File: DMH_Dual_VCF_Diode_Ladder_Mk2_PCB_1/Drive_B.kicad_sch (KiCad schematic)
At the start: 25 parts, among them J17 Conn_01x10_PinHeader, Q1 BC548, Q2 BC548, U1 TL074

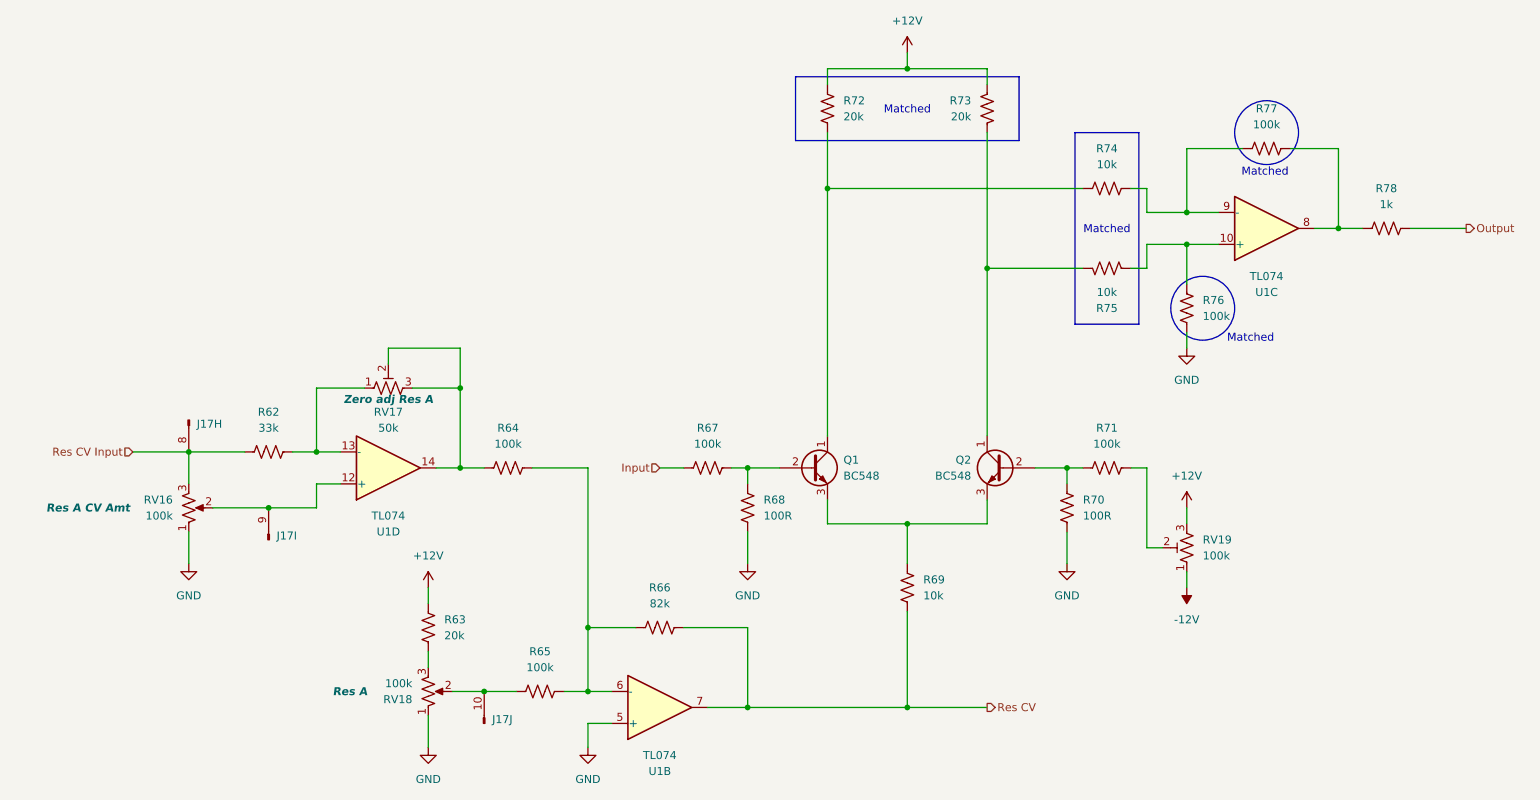
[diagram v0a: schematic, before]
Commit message: Created Drive CV circuits
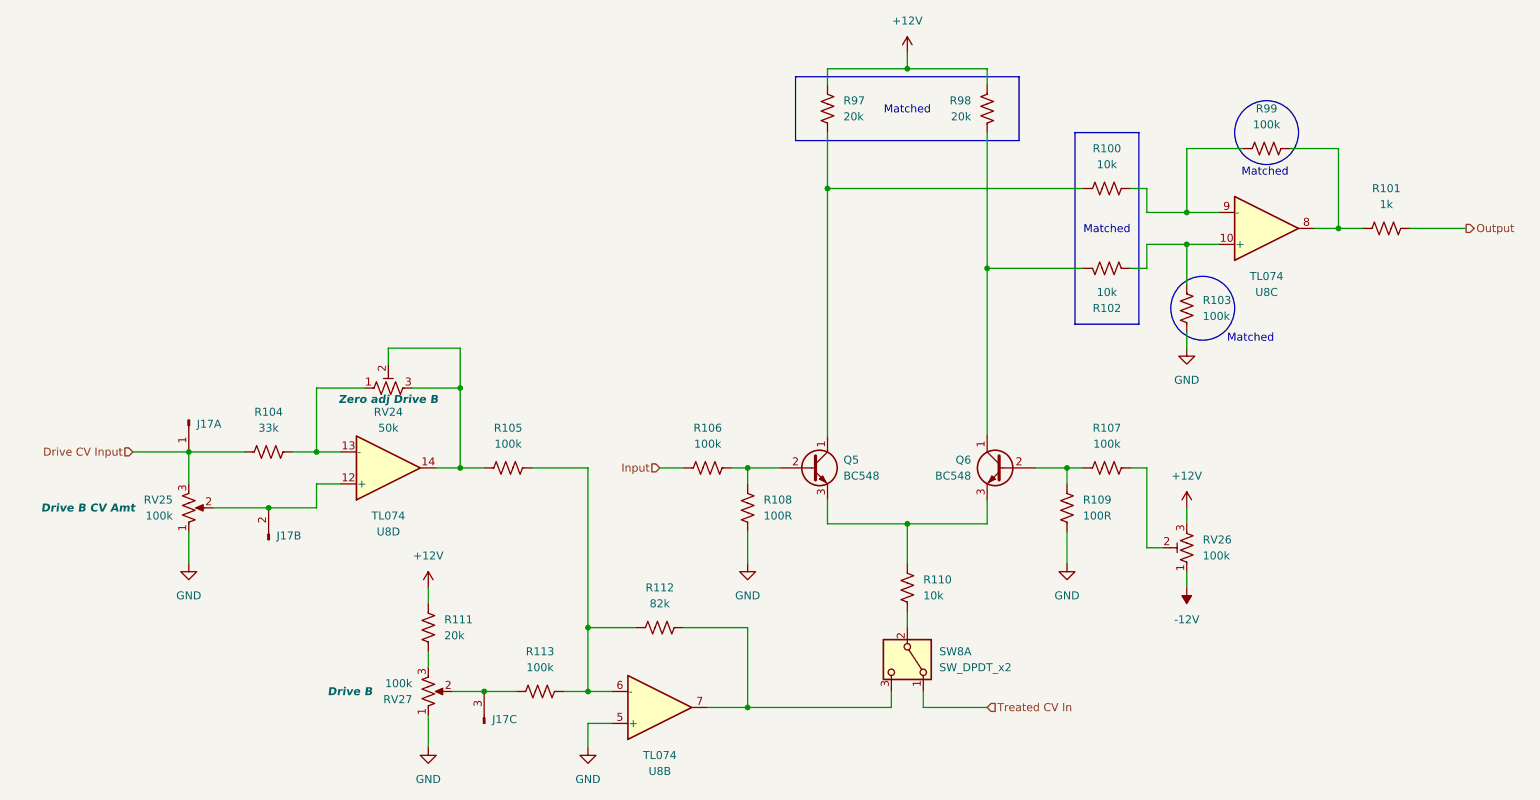
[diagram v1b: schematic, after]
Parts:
- added SW8: SW_DPDT_x2, SynthStuff:Toggle_Switch_2_Poles_TE, symbol Switch:SW_DPDT_x2
- RV24: renamed from RV17; Function Zero adj Res A -> Zero adj Drive B
- RV25: renamed from RV16; Function Res A CV Amt -> Drive B CV Amt
- RV27: renamed from RV18; Function Res A -> Drive B
- renumbered Q1 to Q5, Q2 to Q6, R74 to R100, R78 to R101, R75 to R102, R76 to R103, R62 to R104, R64 to R105, R67 to R106, R71 to R107, R68 to R108, R70 to R109, R69 to R110, R63 to R111, R66 to R112, R65 to R113, R72 to R97, R73 to R98, R77 to R99, RV19 to RV26, U1 to U8
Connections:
- net at R113.1, RV27.2: now also J17.3 (Pin_3); no longer J17.10 (Pin_10)
- net at RV25.2, U8.12 (+): now also J17.2 (Pin_2); no longer J17.9 (Pin_9)
- net Res CV: no longer names the net of R112.2, U8.7
- net Res CV: now also SW8.3 (C); no longer R110.1
- net Res CV Input renamed Drive CV Input
- net Drive CV Input: now also J17.1 (Pin_1); no longer J17.8 (Pin_8)
- new net: R110.1, SW8.2 (B)
- new net Treated CV In: SW8.1 (A)

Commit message: Added inter-board pins to all circuits
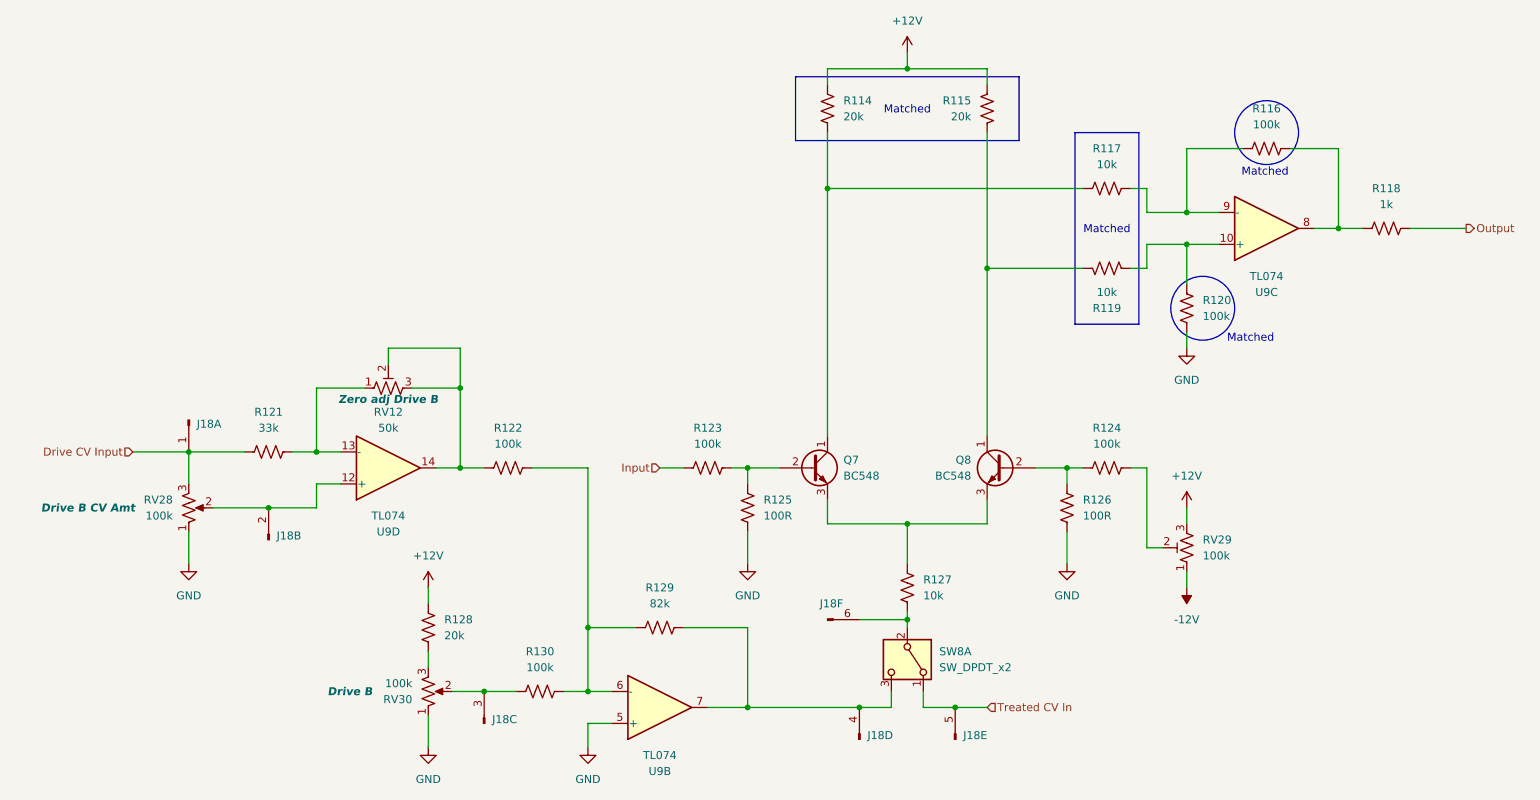
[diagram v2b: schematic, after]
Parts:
- added unit 4 of J18
- added unit 6 of J18
- added unit 5 of J18
- J18: renamed from J17; value Conn_01x10_PinHeader -> Conn_01x06_PinHeader; symbol SynthStuff:Conn_01x10_PinHeader -> SynthStuff:Conn_01x06_PinHeader
- renumbered Q5 to Q7, Q6 to Q8, R97 to R114, R98 to R115, R99 to R116, R100 to R117, R101 to R118, R102 to R119, R103 to R120, R104 to R121, R105 to R122, R106 to R123, R107 to R124, R108 to R125, R109 to R126, R110 to R127, R111 to R128, R112 to R129, R113 to R130, RV24 to RV12, RV25 to RV28, RV26 to RV29, RV27 to RV30, U8 to U9
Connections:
- net Treated CV In: now also J18.5 (Pin_5)
- net at R129.2, SW8.3 (C), U9.7: now also J18.4 (Pin_4)
- net at R127.1, SW8.2 (B): now also J18.6 (Pin_6)

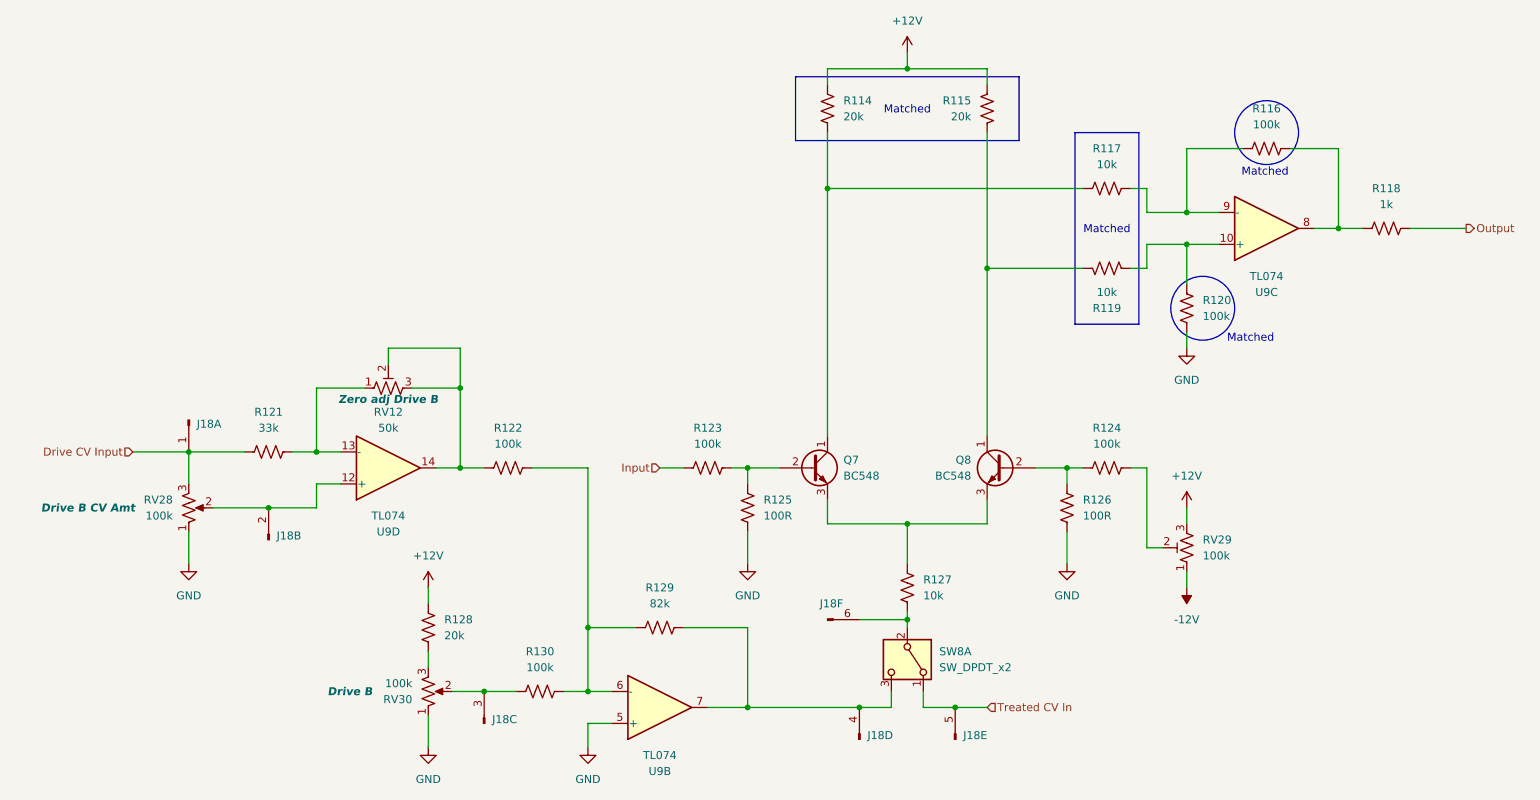
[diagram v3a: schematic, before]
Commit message: Reannotated OpAmps and cleared errors
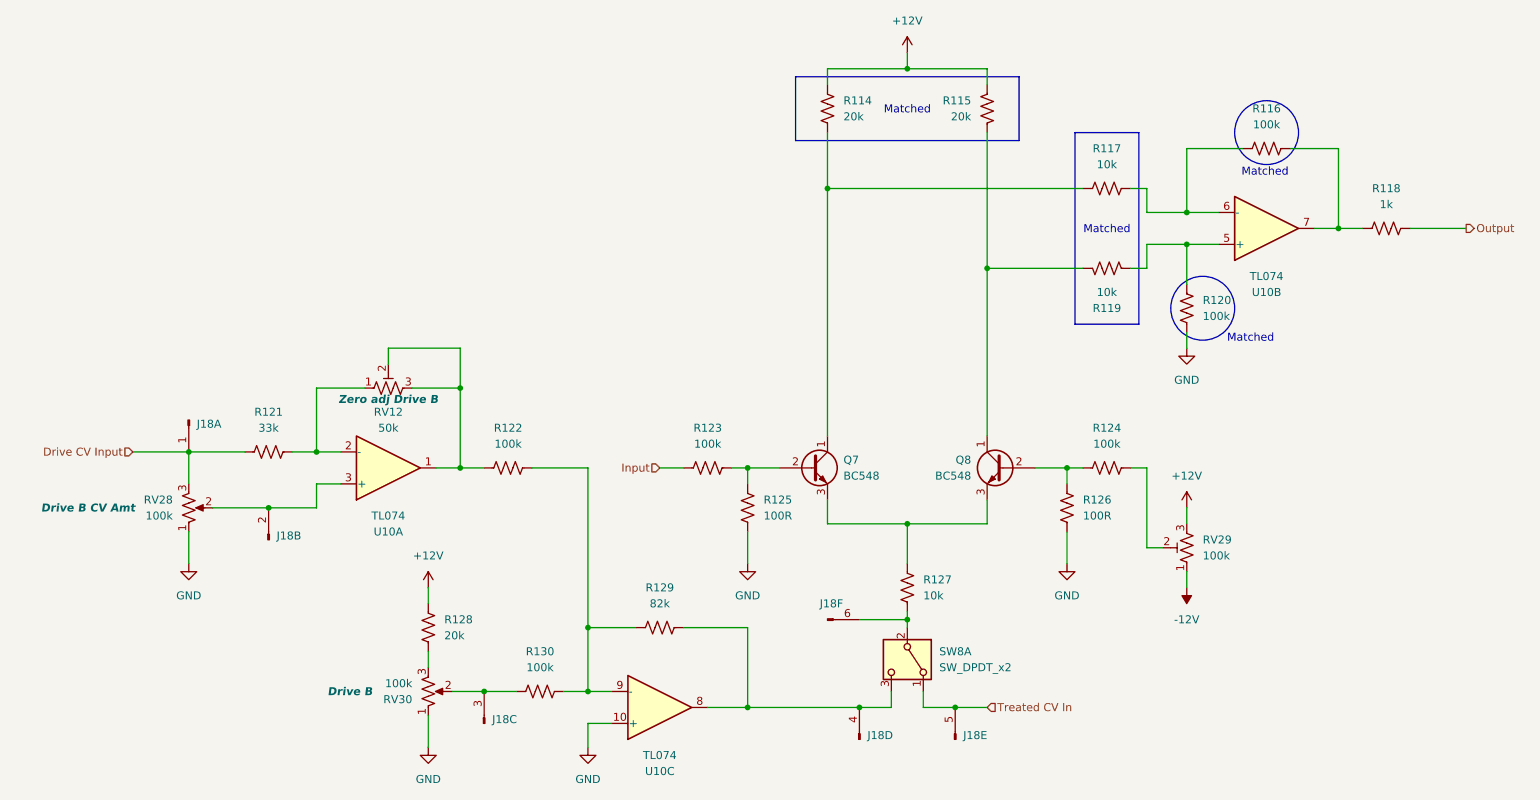
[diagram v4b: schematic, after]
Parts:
- removed U9: TL074, Package_DIP:DIP-14_W7.62mm_Socket, symbol Amplifier_Operational:TL074
- added U10: TL074, Package_DIP:DIP-14_W7.62mm_Socket, symbol Amplifier_Operational:TL074
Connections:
- net GND: now also U10.10 (+)
- net at R122.2, R129.1, R130.2: now also U10.9 (-)
- net at J18.4 (Pin_4), R129.2, SW8.3 (C): now also U10.8
- net at R121.2, RV12.1: now also U10.2 (-)
- net at R122.1, RV12.2, RV12.3: now also U10.1
- net at R119.1, R120.1: now also U10.5 (+)
- net at R116.1, R118.2: now also U10.7
- net at R116.2, R117.1: now also U10.6 (-)
- net at J18.2 (Pin_2), RV28.2: now also U10.3 (+)
